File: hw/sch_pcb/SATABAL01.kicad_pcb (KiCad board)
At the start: 2 copper layers, 40.6 x 30.5 mm, 9 parts, among them J1 SATA7-67491-1030, J2 Conn_Coaxial SMA or MCX, J3 Conn_Coaxial SMA or MCX, T1 ETC1-1-13, T2 ETC1-1-13

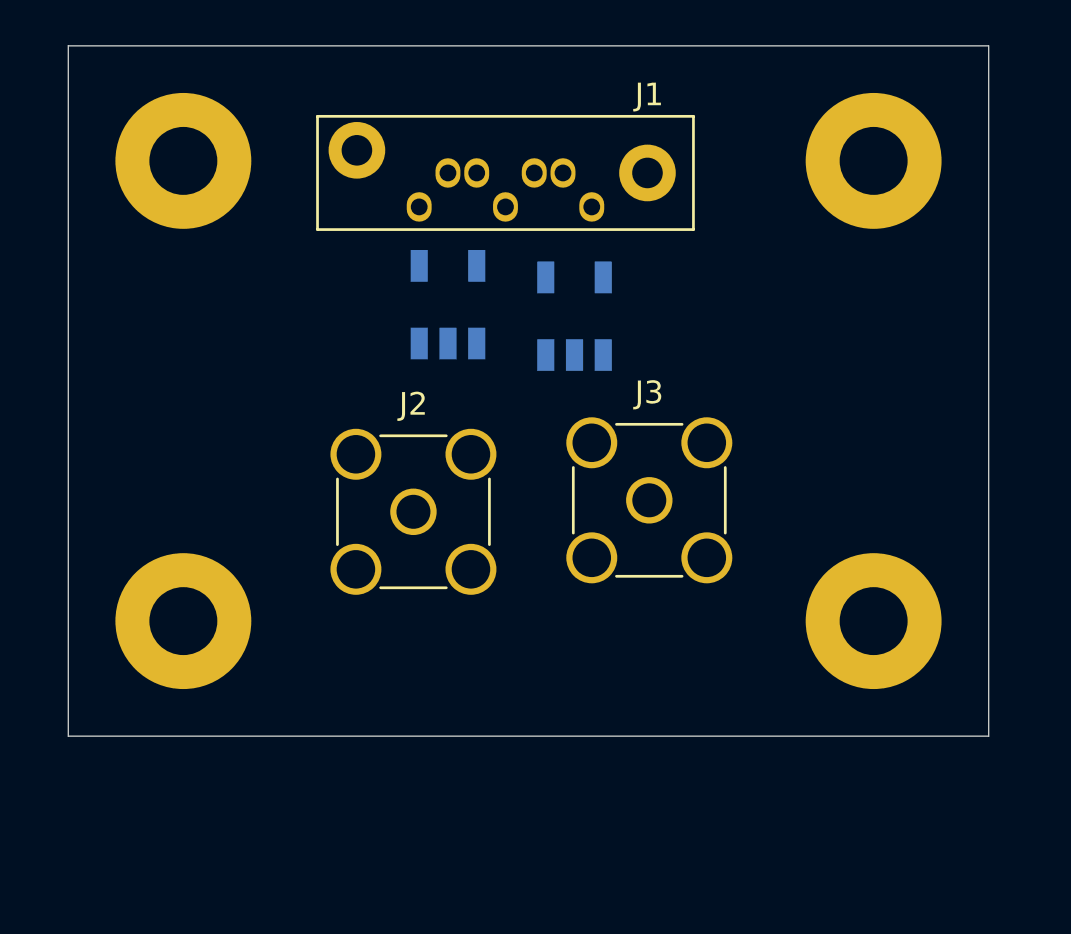
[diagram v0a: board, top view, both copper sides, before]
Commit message: Fix issue in ground connection.
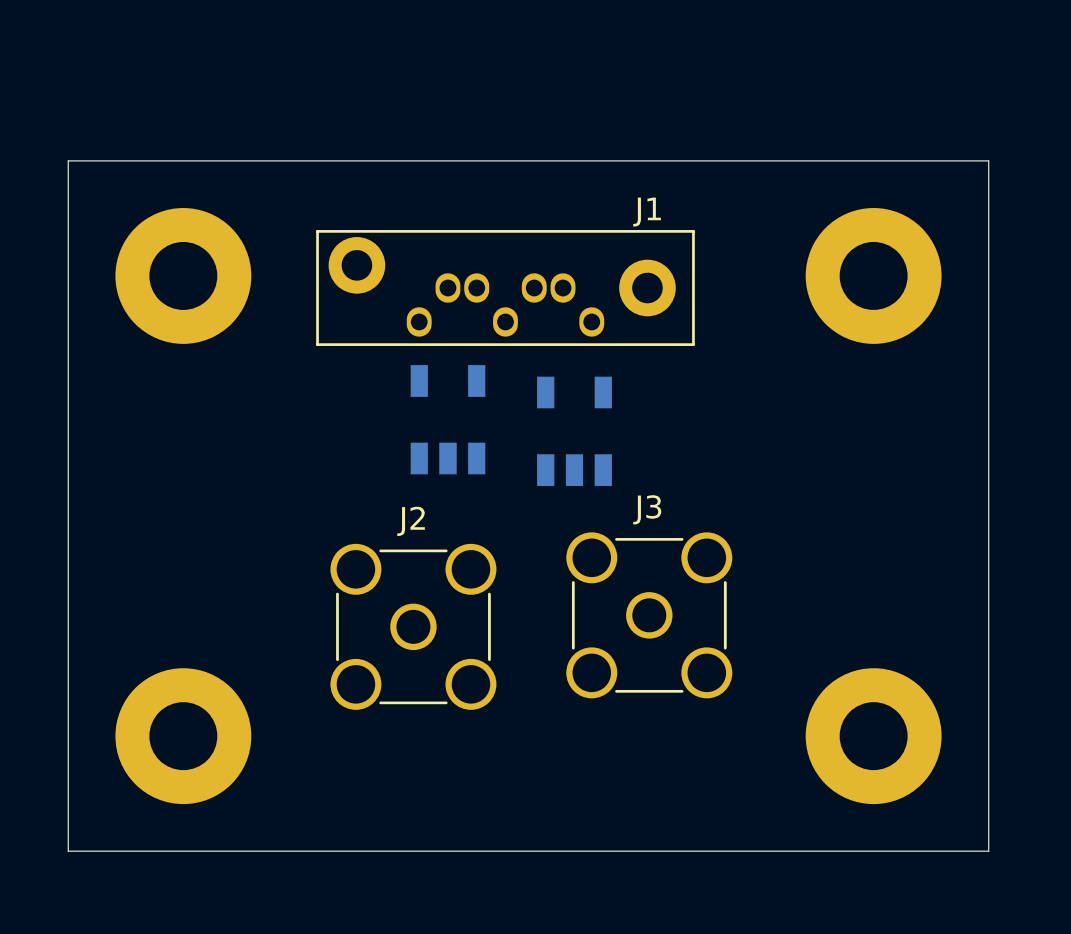
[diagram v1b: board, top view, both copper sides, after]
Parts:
- moved H2 5.08 mm to (5.08, -25.4)
- moved H4 5.08 mm to (35.6, -25.4)
- moved J1 5.08 mm to (23.1, -23.4)
- moved H1 5.08 mm to (5.08, -5.08)
- moved H3 5.08 mm to (35.6, -5.08)
- moved J2 5.08 mm to (15.2, -9.91)
- moved J3 5.08 mm to (25.7, -10.4)
- moved T1 5.08 mm to (22.4, -18.5)
- moved T2 5.08 mm to (16.8, -19.1)
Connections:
- H1 pad 1: /IN1 -> GND
- H2 pad 1: /IN2 -> GND
- H3 pad 1: /IN1 -> GND
- H4 pad 1: /IN2 -> GND
- J1 pad 1: DGND -> GND
- J1 pad 4: DGND -> GND
- J1 pad 7: DGND -> GND
- J1 pad 8: DGND -> GND
- J1 pad 9: DGND -> GND

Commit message: Layout improvement Add module metadata.
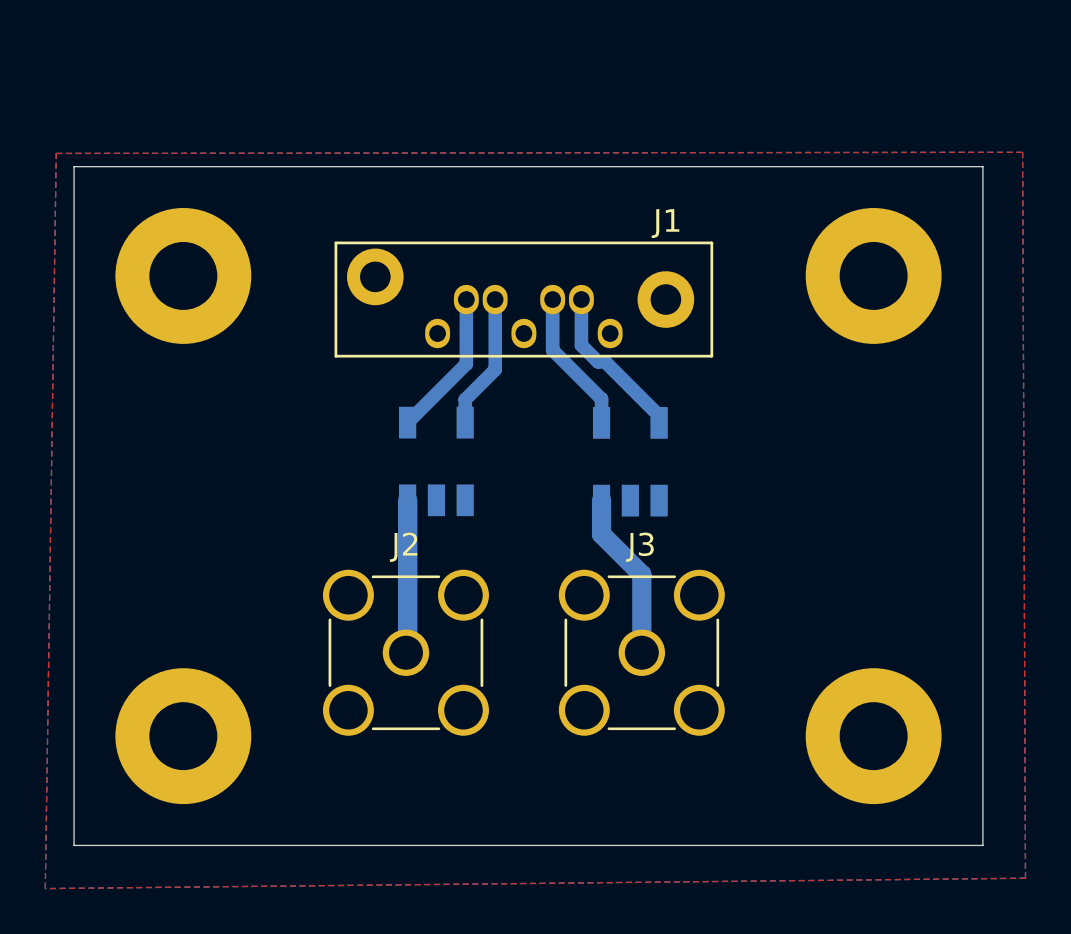
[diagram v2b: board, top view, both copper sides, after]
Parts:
- moved T1 2.81 mm to (24.8, -17.2)
- moved T2 1.91 mm to (16.3, -17.2)
- moved J3 1.68 mm to (25.3, -8.76)
- moved J2 1.19 mm to (14.9, -8.76)
- moved J1 0.96 mm to (23.9, -22.9)
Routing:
- net /OUT1: track 0.00 -> 7.45 mm
- net /IN1N: track 0.00 -> 7.06 mm
- net /OUT2: track 0.00 -> 6.76 mm
- net /IN2P: track 0.00 -> 6.51 mm
- net /IN1P: track 0.00 -> 6.34 mm
- net /IN2N: track 0.00 -> 5.98 mm
- added copper zone on B.Cu, net GND
- added copper zone on F.Cu, net GND
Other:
- board size 40.6 x 30.5 mm -> 40.1 x 30 mm
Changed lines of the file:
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@@
   )
   (setup
+    (stackup
+      (layer "F.SilkS" (type "Top Silk Screen"))
+      (layer "F.Paste" (type "Top Solder Paste"))
+      (layer "F.Mask" (type "Top Solder Mask") (color "Green") (thickness 0.01))
+      (layer "F.Cu" (type "copper") (thickness 0.035))
+      (layer "dielectric 1" (type "core") (thickness 1.51) (material "FR4") (epsilon_r 4.5) (loss_tangent 0.02))
+      (layer "B.Cu" (type "copper") (thickness 0.035))
+      (layer "B.Mask" (type "Bottom Solder Mask") (color "Green") (thickness 0.01))
+      (layer "B.Paste" (type "Bottom Solder Paste"))
+      (layer "B.SilkS" (type "Bottom Silk Screen"))
+      (copper_finish "None")
+      (dielectric_constraints no)
+    )
     (pad_to_mask_clearance 0)
     (pcbplotparams
@@
   (net 9 "unconnected-(T2-Pad4)")
   (footprint "Mlab_CON:SATA-7_THT_VERT_2" (layer "F.Cu")
-    (at 23.114 -23.368)
+    (at 23.9268 -22.8586)
     (property "Sheetfile" "SATABAL01.kicad_sch")
     (property "Sheetname" "")
@@
   )
   (footprint "Connector_Coaxial:SMA_Amphenol_901-144_Vertical" (layer "F.Cu")
-    (at 15.24 -9.906)
+    (at 14.9098 -8.763)
     (descr "https://www.amphenolrf.com/downloads/dl/file/id/7023/product/3103/901_144_customer_drawing.pdf")
     (tags "SMA THT Female Jack Vertical")
@@
     )
   )
-  (footprint "Mlab_Mechanical:MountingHole_3mm" placed (layer "F.Cu")
+  (footprint "Mlab_Mechanical:MountingHole_3mm" locked placed (layer "F.Cu")
     (at 35.56 -25.4)
     (descr "Mounting hole, Befestigungsbohrung, 3mm, No Annular, Kein Restring,")
@@
     )
     (fp_circle (center 0 0) (end 2.99974 0) (layer "F.Fab") (width 0.381) (fill none))
-    (pad "1" thru_hole circle (at 0 0) (size 6 6) (drill 3) (layers *.Cu *.Adhes *.Mask)
+    (pad "1" thru_hole circle locked (at 0 0) (size 6 6) (drill 3) (layers *.Cu *.Adhes *.Mask)
       (net 6 "GND") (pinfunction "1") (pintype "input") (clearance 1) (zone_connect 2))
     (model "${MLAB}/src/3d/mechanical/m3_komplet.step"
@@
   )
   (footprint "Connector_Coaxial:SMA_Amphenol_901-144_Vertical" (layer "F.Cu")
-    (at 25.654 -10.414)
+    (at 25.3238 -8.763)
     (descr "https://www.amphenolrf.com/downloads/dl/file/id/7023/product/3103/901_144_customer_drawing.pdf")
     (tags "SMA THT Female Jack Vertical")
@@
     )
   )
-  (footprint "Mlab_Mechanical:MountingHole_3mm" placed (layer "F.Cu")
+  (footprint "Mlab_Mechanical:MountingHole_3mm" locked placed (layer "F.Cu")
     (at 35.56 -5.08)
     (descr "Mounting hole, Befestigungsbohrung, 3mm, No Annular, Kein Restring,")
@@
     )
     (fp_circle (center 0 0) (end 2.99974 0) (layer "F.Fab") (width 0.381) (fill none))
-    (pad "1" thru_hole circle (at 0 0) (size 6 6) (drill 3) (layers *.Cu *.Adhes *.Mask)
+    (pad "1" thru_hole circle locked (at 0 0) (size 6 6) (drill 3) (layers *.Cu *.Adhes *.Mask)
       (net 6 "GND") (pinfunction "1") (pintype "input") (clearance 1) (zone_connect 2))
     (model "${MLAB}/src/3d/mechanical/m3_komplet.step"
@@
     )
   )
-  (footprint "Mlab_Mechanical:MountingHole_3mm" placed (layer "F.Cu")
+  (footprint "Mlab_Mechanical:MountingHole_3mm" locked placed (layer "F.Cu")
     (at 5.08 -25.4)
     (descr "Mounting hole, Befestigungsbohrung, 3mm, No Annular, Kein Restring,")
@@
     )
     (fp_circle (center 0 0) (end 2.99974 0) (layer "F.Fab") (width 0.381) (fill none))
-    (pad "1" thru_hole circle (at 0 0) (size 6 6) (drill 3) (layers *.Cu *.Adhes *.Mask)
+    (pad "1" thru_hole circle locked (at 0 0) (size 6 6) (drill 3) (layers *.Cu *.Adhes *.Mask)
       (net 6 "GND") (pinfunction "1") (pintype "input") (clearance 1) (zone_connect 2))
     (model "${MLAB}/src/3d/mechanical/m3_komplet.step"
@@
     )
   )
-  (footprint "Mlab_Mechanical:MountingHole_3mm" placed (layer "F.Cu")
+  (footprint "Mlab_Mechanical:MountingHole_3mm" locked placed (layer "F.Cu")
     (at 5.08 -5.08)
     (descr "Mounting hole, Befestigungsbohrung, 3mm, No Annular, Kein Restring,")
@@
     )
     (fp_circle (center 0 0) (end 2.99974 0) (layer "F.Fab") (width 0.381) (fill none))
-    (pad "1" thru_hole circle (at 0 0) (size 6 6) (drill 3) (layers *.Cu *.Adhes *.Mask)
+    (pad "1" thru_hole circle locked (at 0 0) (size 6 6) (drill 3) (layers *.Cu *.Adhes *.Mask)
       (net 6 "GND") (pinfunction "1") (pintype "input") (clearance 1) (zone_connect 2))
     (model "${MLAB}/src/3d/mechanical/m3_komplet.step"
@@
   )
   (footprint "Transformer_SMD:Transformer_MACOM_SM-22" (layer "B.Cu")
-    (at 16.764 -19.05 -90)
+    (at 16.256 -17.209 -90)
     (descr "https://cdn.macom.com/datasheets/ETC1-1-13.pdf")
     (tags "RF Transformer")
@@
   )
   (footprint "Transformer_SMD:Transformer_MACOM_SM-22" (layer "B.Cu")
-    (at 22.352 -18.542 -90)
+    (at 24.8158 -17.1958 -90)
     (descr "https://cdn.macom.com/datasheets/ETC1-1-13.pdf")
     (tags "RF Transformer")
@@
     )
   )
-  (gr_rect (start 0 -30.48) (end 40.64 0) (layer "Edge.Cuts") (width 0.05) (fill none))
+  (gr_rect (start 0.254 -30.226) (end 40.386 -0.254) (layer "Edge.Cuts") (width 0.05) (fill none))
+  (dimension (type aligned) (layer "Dwgs.User")
+    (pts (xy 0.254 -30.226) (xy 40.386 -30.226))
+    (height -2.413)
+    (gr_text "40 mm" (at 20.32 -33.789) (layer "Dwgs.User")
+      (effects (font (size 1 1) (thickness 0.15)))
+    )
+    (format (units 3) (units_format 1) (precision 0))
+    (style (thickness 0.15) (arrow_length 1.27) (text_position_mode 0) (extension_height 0.58642) (extension_offset 0.5) keep_text_aligned)
+  )
+  (dimension (type aligned) (layer "Dwgs.User")
+    (pts (xy 40.386 -0.254) (xy 40.386 -30.226))
+    (height 4.0386)
+    (gr_text "30 mm" (at 43.2746 -15.24 90) (layer "Dwgs.User")
+      (effects (font (size 1 1) (thickness 0.15)))
+    )
+    (format (units 3) (units_format 1) (precision 0))
+    (style (thickness 0.15) (arrow_length 1.27) (text_position_mode 0) (extension_height 0.58642) (extension_offset 0.5) keep_text_aligned)
+  )
+  (dimension (type aligned) (layer "Dwgs.User")
+    (pts (xy 0.254 -30.226) (xy 40.386 -30.226))
+    (height -5.4864)
+    (gr_text "40,13 mm" (at 20.32 -36.8624) (layer "Dwgs.User")
+      (effects (font (size 1 1) (thickness 0.15)))
+    )
+    (format (units 2) (units_format 1) (precision 2))
+    (style (thickness 0.15) (arrow_length 1.27) (text_position_mode 0) (extension_height 0.58642) (extension_offset 0.5) keep_text_aligned)
+  )
+  (dimension (type aligned) (layer "Dwgs.User")
+    (pts (xy 40.386 -0.254) (xy 40.386 -30.226))
+    (height 7.5946)
+    (gr_text "29,97 mm" (at 46.8306 -15.24 90) (layer "Dwgs.User")
+      (effects (font (size 1 1) (thickness 0.15)))
+    )
+    (format (units 2) (units_format 1) (precision 2))
+    (style (thickness 0.15) (arrow_length 1.27) (text_position_mode 0) (extension_height 0.58642) (extension_offset 0.5) keep_text_aligned)
+  )
+  (segment (start 17.5768 -21.5148) (end 17.5768 -24.3586) (width 0.6) (layer "B.Cu") (net 1))
+  (segment (start 17.5768 -21.5148) (end 14.986 -18.924) (width 0.6) (layer "B.Cu") (net 1))
+  (segment (start 18.8468 -21.2598) (end 17.526 -19.939) (width 0.6) (layer "B.Cu") (net 2))
+  (segment (start 17.526 -19.939) (end 17.526 -18.924) (width 0.6) (layer "B.Cu") (net 2))
+  (segment (start 18.8468 -21.2598) (end 18.8468 -24.3586) (width 0.6) (layer "B.Cu") (net 2))
+  (segment (start 21.3868 -22.1234) (end 23.5458 -19.9644) (width 0.6) (layer "B.Cu") (net 3))
+  (segment (start 23.5458 -19.9644) (end 23.5458 -18.9108) (width 0.6) (layer "B.Cu") (net 3))
+  (segment (start 21.3868 -24.3586) (end 21.3868 -22.1234) (width 0.6) (layer "B.Cu") (net 3))
+  (segment (start 23.387519 -21.609081) (end 23.70752 -21.60908) (width 0.6) (layer "B.Cu") (net 4))
+  (segment (start 22.6568 -24.3586) (end 22.6568 -22.3398) (width 0.6) (layer "B.Cu") (net 4))
+  (segment (start 22.6568 -22.3398) (end 23.387519 -21.609081) (width 0.6) (layer "B.Cu") (net 4))
+  (segment (start 26.0858 -19.2308) (end 26.0858 -18.9108) (width 0.6) (layer "B.Cu") (net 4))
+  (segment (start 23.70752 -21.60908) (end 26.0858 -19.2308) (width 0.6) (layer "B.Cu") (net 4))
+  (segment (start 14.986 -15.494) (end 14.986 -8.8392) (width 0.85) (layer "B.Cu") (net 5))
+  (segment (start 14.986 -8.8392) (end 14.9098 -8.763) (width 0.85) (layer "B.Cu") (net 5))
+  (segment (start 25.3238 -12.2174) (end 25.3238 -8.763) (width 0.85) (layer "B.Cu") (net 7))
+  (segment (start 23.5458 -15.4808) (end 23.5458 -13.9954) (width 0.85) (layer "B.Cu") (net 7))
+  (segment (start 23.5458 -13.9954) (end 25.3238 -12.2174) (width 0.85) (layer "B.Cu") (net 7))
+  (zone (net 6) (net_name "GND") (layers F&B.Cu) (hatch edge 0.508)
+    (connect_pads (clearance 0.25))
+    (min_thickness 0.254) (filled_areas_thickness no)
+    (fill yes (thermal_gap 0.508) (thermal_bridge_width 0.508))
+    (polygon
+      (pts
+        (xy 42.2656 1.1938)
+        (xy -1.016 1.651)
+        (xy -0.5334 -30.8102)
+        (xy 42.1386 -30.861)
+      )
+    )
+  )
 )

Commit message: Improve silkscreen.
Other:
- board text added: "Kaklik 2021"
- board text added: "MLAB.cz"
- board text added: "SATABAL01A"
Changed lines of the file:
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@@
   )
   (gr_rect (start 0.254 -30.226) (end 40.386 -0.254) (layer "Edge.Cuts") (width 0.05) (fill none))
+  (gr_text "MLAB.cz" (at 35.2298 -15.7226 90) (layer "F.SilkS")
+    (effects (font (size 1 1) (thickness 0.15)))
+  )
+  (gr_text "Kaklik 2021" (at 37.592 -15.7226 90) (layer "F.SilkS")
+    (effects (font (size 1 1) (thickness 0.15)))
+  )
+  (gr_text "SATABAL01A" (at 33.147 -15.1638 90) (layer "F.SilkS")
+    (effects (font (size 1 1) (thickness 0.15)))
+  )
   (dimension (type aligned) (layer "Dwgs.User")
     (pts (xy 0.254 -30.226) (xy 40.386 -30.226))
     (height -2.413)
-    (gr_text "40 mm" (at 20.32 -33.789) (layer "Dwgs.User")
+    (gr_text "1580 mils" (at 20.32 -33.789) (layer "Dwgs.User")
       (effects (font (size 1 1) (thickness 0.15)))
     )
@@
     (pts (xy 40.386 -0.254) (xy 40.386 -30.226))
     (height 4.0386)
-    (gr_text "30 mm" (at 43.2746 -15.24 90) (layer "Dwgs.User")
+    (gr_text "1180 mils" (at 43.2746 -15.24 90) (layer "Dwgs.User")
       (effects (font (size 1 1) (thickness 0.15)))
     )
@@
     (pts (xy 0.254 -30.226) (xy 40.386 -30.226))
     (height -5.4864)
-    (gr_text "40,13 mm" (at 20.32 -36.8624) (layer "Dwgs.User")
+    (gr_text "40.13 mm" (at 20.32 -36.8624) (layer "Dwgs.User")
       (effects (font (size 1 1) (thickness 0.15)))
     )
@@
     (pts (xy 40.386 -0.254) (xy 40.386 -30.226))
     (height 7.5946)
-    (gr_text "29,97 mm" (at 46.8306 -15.24 90) (layer "Dwgs.User")
+    (gr_text "29.97 mm" (at 46.8306 -15.24 90) (layer "Dwgs.User")
       (effects (font (size 1 1) (thickness 0.15)))
     )

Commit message: Minor silkscreen and layout improvements.
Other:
- board text added: "Ch1"
- board text added: "Ch2"
- board text added: "www.mlab.cz"
- board text removed: "MLAB.cz"
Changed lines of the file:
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@@
     (property "Sheetfile" "SATABAL01.kicad_sch")
     (property "Sheetname" "")
-    (fp_text reference "J1" (at 2.54 -4.953) (layer "F.SilkS")
+    (fp_text reference "J1" (at 5.8166 -0.738) (layer "F.SilkS")
       (effects (font (size 1 1) (thickness 0.15)))
     )
@@
   )
   (gr_rect (start 0.254 -30.226) (end 40.386 -0.254) (layer "Edge.Cuts") (width 0.05) (fill none))
-  (gr_text "MLAB.cz" (at 35.2298 -15.7226 90) (layer "F.SilkS")
-    (effects (font (size 1 1) (thickness 0.15)))
-  )
-  (gr_text "Kaklik 2021" (at 37.592 -15.7226 90) (layer "F.SilkS")
-    (effects (font (size 1 1) (thickness 0.15)))
-  )
-  (gr_text "SATABAL01A" (at 33.147 -15.1638 90) (layer "F.SilkS")
-    (effects (font (size 1 1) (thickness 0.15)))
+  (gr_text "Ch1" (at 16.0274 -28.3464) (layer "F.SilkS")
+    (effects (font (size 1.3 1.3) (thickness 0.3)))
+  )
+  (gr_text "Ch2" (at 25.4 -2.6416) (layer "F.SilkS")
+    (effects (font (size 1.3 1.3) (thickness 0.3)))
+  )
+  (gr_text "Ch1" (at 14.7828 -2.6416) (layer "F.SilkS")
+    (effects (font (size 1.3 1.3) (thickness 0.3)))
+  )
+  (gr_text "www.mlab.cz" (at 30.607 -15.621 90) (layer "F.SilkS")
+    (effects (font (size 1.3 1.3) (thickness 0.3)))
+  )
+  (gr_text "Kaklik 2021" (at 33.0454 -15.5702 90) (layer "F.SilkS")
+    (effects (font (size 1.3 1.3) (thickness 0.3)))
+  )
+  (gr_text "Ch2" (at 24.0538 -28.3464) (layer "F.SilkS")
+    (effects (font (size 1.3 1.3) (thickness 0.3)))
+  )
+  (gr_text "SATABAL01A" (at 20.4216 -17.145) (layer "F.SilkS")
+    (effects (font (size 1.5 1.5) (thickness 0.3)))
   )
   (dimension (type aligned) (layer "Dwgs.User")
@@
       (effects (font (size 1 1) (thickness 0.15)))
     )
-    (format (units 3) (units_format 1) (precision 0))
+    (format (units 1) (units_format 1) (precision 0))
     (style (thickness 0.15) (arrow_length 1.27) (text_position_mode 0) (extension_height 0.58642) (extension_offset 0.5) keep_text_aligned)
   )
@@
       (effects (font (size 1 1) (thickness 0.15)))
     )
-    (format (units 3) (units_format 1) (precision 0))
+    (format (units 1) (units_format 1) (precision 0))
     (style (thickness 0.15) (arrow_length 1.27) (text_position_mode 0) (extension_height 0.58642) (extension_offset 0.5) keep_text_aligned)
   )
@@
   (segment (start 23.5458 -19.9644) (end 23.5458 -18.9108) (width 0.6) (layer "B.Cu") (net 3))
   (segment (start 21.3868 -24.3586) (end 21.3868 -22.1234) (width 0.6) (layer "B.Cu") (net 3))
-  (segment (start 23.387519 -21.609081) (end 23.70752 -21.60908) (width 0.6) (layer "B.Cu") (net 4))
-  (segment (start 22.6568 -24.3586) (end 22.6568 -22.3398) (width 0.6) (layer "B.Cu") (net 4))
-  (segment (start 22.6568 -22.3398) (end 23.387519 -21.609081) (width 0.6) (layer "B.Cu") (net 4))
-  (segment (start 26.0858 -19.2308) (end 26.0858 -18.9108) (width 0.6) (layer "B.Cu") (net 4))
-  (segment (start 23.70752 -21.60908) (end 26.0858 -19.2308) (width 0.6) (layer "B.Cu") (net 4))
+  (segment (start 22.6568 -22.1996) (end 24.8793 -19.9771) (width 0.6) (layer "B.Cu") (net 4))
+  (segment (start 25.3619 -19.9771) (end 24.8793 -19.9771) (width 0.6) (layer "B.Cu") (net 4))
+  (segment (start 26.0858 -18.9108) (end 26.0858 -19.2532) (width 0.6) (layer "B.Cu") (net 4))
+  (segment (start 26.0858 -19.2532) (end 25.3619 -19.9771) (width 0.6) (layer "B.Cu") (net 4))
+  (segment (start 22.6568 -24.3586) (end 22.6568 -22.1996) (width 0.6) (layer "B.Cu") (net 4))
   (segment (start 14.986 -15.494) (end 14.986 -8.8392) (width 0.85) (layer "B.Cu") (net 5))
   (segment (start 14.986 -8.8392) (end 14.9098 -8.763) (width 0.85) (layer "B.Cu") (net 5))
